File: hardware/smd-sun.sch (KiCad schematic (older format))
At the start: 18 parts, among them U1 NE555, U2 4017

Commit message: Rename all to smd-sun
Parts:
- BT1: symbol smd-star:BK-883 -> smd-sun:BK-883
- C1, C2: footprint smd-star:C_0805_2012Metric_Pad1.15x1.40mm_HandSolder -> smd-sun:C_0805_2012Metric_Pad1.15x1.40mm_HandSolder; symbol smd-star:C -> smd-sun:C
- D1, D10, D2, D3, D4, D5, D6, D7, D8, D9: footprint smd-star:LED_0805_2012Metric_Pad1.15x1.40mm_HandSolder -> smd-sun:LED_0805_2012Metric_Pad1.15x1.40mm_HandSolder; symbol smd-star:LED -> smd-sun:LED
- R1, R2, R3: footprint smd-star:R_0805_2012Metric_Pad1.15x1.40mm_HandSolder -> smd-sun:R_0805_2012Metric_Pad1.15x1.40mm_HandSolder; symbol smd-star:R -> smd-sun:R
- U1: footprint smd-star:SO-8_3.9x4.9mm_P1.27mm -> smd-sun:SO-8_3.9x4.9mm_P1.27mm; symbol smd-star:NE555 -> smd-sun:NE555
- U2: footprint smd-star:SOIC-16_3.9x9.9mm_P1.27mm -> smd-sun:SOIC-16_3.9x9.9mm_P1.27mm; symbol smd-star:4017 -> smd-sun:4017
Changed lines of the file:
@@
 $EndDescr
 $Comp
-L smd-star:NE555 U1
+L smd-sun:NE555 U1
 U 1 1 5EFD01E2
 P 3600 3350
 F 0 "U1" H 3850 3700 50  0000 C CNN
 F 1 "NE555" H 3250 3700 50  0000 C CNN
-F 2 "smd-star:SO-8_3.9x4.9mm_P1.27mm" H 3600 3350 50  0001 C CNN
+F 2 "smd-sun:SO-8_3.9x4.9mm_P1.27mm" H 3600 3350 50  0001 C CNN
 F 3 "http://www.ti.com/lit/ds/symlink/ne555.pdf" H 3600 3350 50  0001 C CNN
 	1    3600 3350
@@
 $EndComp
 $Comp
-L smd-star:4017 U2
+L smd-sun:4017 U2
 U 1 1 5EFD0D05
 P 5650 3650
 F 0 "U2" H 5900 4300 50  0000 C CNN
 F 1 "4017" H 5400 4300 50  0000 C CNN
-F 2 "smd-star:SOIC-16_3.9x9.9mm_P1.27mm" H 5650 3650 50  0001 C CNN
+F 2 "smd-sun:SOIC-16_3.9x9.9mm_P1.27mm" H 5650 3650 50  0001 C CNN
 F 3 "http://www.intersil.com/content/dam/Intersil/documents/cd40/cd4017bms-22bms.pdf" H 5650 3650 50  0001 C CNN
 	1    5650 3650
@@
 	2900 3150 3100 3150
 $Comp
-L smd-star:R R1
+L smd-sun:R R1
 U 1 1 5EFD9130
 P 4600 2900
 F 0 "R1" H 4670 2946 50  0000 L CNN
 F 1 "47k" H 4670 2855 50  0000 L CNN
-F 2 "smd-star:R_0805_2012Metric_Pad1.15x1.40mm_HandSolder" V 4530 2900 50  0001 C CNN
+F 2 "smd-sun:R_0805_2012Metric_Pad1.15x1.40mm_HandSolder" V 4530 2900 50  0001 C CNN
 F 3 "~" H 4600 2900 50  0001 C CNN
 	1    4600 2900
@@
 $EndComp
 $Comp
-L smd-star:R R2
+L smd-sun:R R2
 U 1 1 5EFDA69B
 P 4600 3650
 F 0 "R2" H 4670 3696 50  0000 L CNN
 F 1 "47k" H 4670 3605 50  0000 L CNN
-F 2 "smd-star:R_0805_2012Metric_Pad1.15x1.40mm_HandSolder" V 4530 3650 50  0001 C CNN
+F 2 "smd-sun:R_0805_2012Metric_Pad1.15x1.40mm_HandSolder" V 4530 3650 50  0001 C CNN
 F 3 "~" H 4600 3650 50  0001 C CNN
 	1    4600 3650
@@
 $EndComp
 $Comp
-L smd-star:C C1
+L smd-sun:C C1
 U 1 1 5EFDAF79
 P 2800 4050
 F 0 "C1" H 2400 4100 50  0000 L CNN
 F 1 "0.01uF" H 2400 4000 50  0000 L CNN
-F 2 "smd-star:C_0805_2012Metric_Pad1.15x1.40mm_HandSolder" H 2838 3900 50  0001 C CNN
+F 2 "smd-sun:C_0805_2012Metric_Pad1.15x1.40mm_HandSolder" H 2838 3900 50  0001 C CNN
 F 3 "~" H 2800 4050 50  0001 C CNN
 	1    2800 4050
@@
 $EndComp
 $Comp
-L smd-star:C C2
+L smd-sun:C C2
 U 1 1 5EFDE976
 P 4600 4050
 F 0 "C2" H 4715 4096 50  0000 L CNN
 F 1 "10uF" H 4715 4005 50  0000 L CNN
-F 2 "smd-star:C_0805_2012Metric_Pad1.15x1.40mm_HandSolder" H 4638 3900 50  0001 C CNN
+F 2 "smd-sun:C_0805_2012Metric_Pad1.15x1.40mm_HandSolder" H 4638 3900 50  0001 C CNN
 F 3 "~" H 4600 4050 50  0001 C CNN
 	1    4600 4050
@@
 	5650 2750 5650 2850
 $Comp
-L smd-star:LED D8
+L smd-sun:LED D8
 U 1 1 5EFF47F1
 P 7200 4200
 F 0 "D8" V 7300 4200 50  0000 R CNN
 F 1 "LED" V 7148 4083 50  0001 R CNN
-F 2 "smd-star:LED_0805_2012Metric_Pad1.15x1.40mm_HandSolder" H 7200 4200 50  0001 C CNN
+F 2 "smd-sun:LED_0805_2012Metric_Pad1.15x1.40mm_HandSolder" H 7200 4200 50  0001 C CNN
 F 3 "~" H 7200 4200 50  0001 C CNN
 	1    7200 4200
@@
 $EndComp
 $Comp
-L smd-star:LED D6
+L smd-sun:LED D6
 U 1 1 5EFF6FCA
 P 7600 4200
 F 0 "D6" V 7700 4200 50  0000 R CNN
 F 1 "LED" V 7548 4083 50  0001 R CNN
-F 2 "smd-star:LED_0805_2012Metric_Pad1.15x1.40mm_HandSolder" H 7600 4200 50  0001 C CNN
+F 2 "smd-sun:LED_0805_2012Metric_Pad1.15x1.40mm_HandSolder" H 7600 4200 50  0001 C CNN
 F 3 "~" H 7600 4200 50  0001 C CNN
 	1    7600 4200
@@
 $EndComp
 $Comp
-L smd-star:LED D5
+L smd-sun:LED D5
 U 1 1 5EFF7386
 P 7800 4200
 F 0 "D5" V 7900 4200 50  0000 R CNN
 F 1 "LED" V 7748 4083 50  0001 R CNN
-F 2 "smd-star:LED_0805_2012Metric_Pad1.15x1.40mm_HandSolder" H 7800 4200 50  0001 C CNN
+F 2 "smd-sun:LED_0805_2012Metric_Pad1.15x1.40mm_HandSolder" H 7800 4200 50  0001 C CNN
 F 3 "~" H 7800 4200 50  0001 C CNN
 	1    7800 4200
@@
 $EndComp
 $Comp
-L smd-star:LED D4
+L smd-sun:LED D4
 U 1 1 5EFF91CC
 P 8000 4200
 F 0 "D4" V 8100 4200 50  0000 R CNN
 F 1 "LED" V 7948 4083 50  0001 R CNN
-F 2 "smd-star:LED_0805_2012Metric_Pad1.15x1.40mm_HandSolder" H 8000 4200 50  0001 C CNN
+F 2 "smd-sun:LED_0805_2012Metric_Pad1.15x1.40mm_HandSolder" H 8000 4200 50  0001 C CNN
 F 3 "~" H 8000 4200 50  0001 C CNN
 	1    8000 4200
@@
 $EndComp
 $Comp
-L smd-star:LED D3
+L smd-sun:LED D3
 U 1 1 5EFF91D6
 P 8200 4200
 F 0 "D3" V 8300 4200 50  0000 R CNN
 F 1 "LED" V 8148 4083 50  0001 R CNN
-F 2 "smd-star:LED_0805_2012Metric_Pad1.15x1.40mm_HandSolder" H 8200 4200 50  0001 C CNN
+F 2 "smd-sun:LED_0805_2012Metric_Pad1.15x1.40mm_HandSolder" H 8200 4200 50  0001 C CNN
 F 3 "~" H 8200 4200 50  0001 C CNN
 	1    8200 4200
@@
 $EndComp
 $Comp
-L smd-star:LED D2
+L smd-sun:LED D2
 U 1 1 5EFF91E0
 P 8400 4200
 F 0 "D2" V 8500 4200 50  0000 R CNN
 F 1 "LED" V 8348 4083 50  0001 R CNN
-F 2 "smd-star:LED_0805_2012Metric_Pad1.15x1.40mm_HandSolder" H 8400 4200 50  0001 C CNN
+F 2 "smd-sun:LED_0805_2012Metric_Pad1.15x1.40mm_HandSolder" H 8400 4200 50  0001 C CNN
 F 3 "~" H 8400 4200 50  0001 C CNN
 	1    8400 4200
@@
 $EndComp
 $Comp
-L smd-star:LED D1
+L smd-sun:LED D1
 U 1 1 5EFF91EA
 P 8600 4200
 F 0 "D1" V 8700 4200 50  0000 R CNN
 F 1 "LED" V 8548 4083 50  0001 R CNN
-F 2 "smd-star:LED_0805_2012Metric_Pad1.15x1.40mm_HandSolder" H 8600 4200 50  0001 C CNN
+F 2 "smd-sun:LED_0805_2012Metric_Pad1.15x1.40mm_HandSolder" H 8600 4200 50  0001 C CNN
 F 3 "~" H 8600 4200 50  0001 C CNN
 	1    8600 4200
@@
 	7400 4450 7600 4450
 $Comp
-L smd-star:R R3
+L smd-sun:R R3
 U 1 1 5F0080E1
 P 6800 4600
 F 0 "R3" H 6870 4646 50  0000 L CNN
 F 1 "220R" H 6870 4555 50  0000 L CNN
-F 2 "smd-star:R_0805_2012Metric_Pad1.15x1.40mm_HandSolder" V 6730 4600 50  0001 C CNN
+F 2 "smd-sun:R_0805_2012Metric_Pad1.15x1.40mm_HandSolder" V 6730 4600 50  0001 C CNN
 F 3 "~" H 6800 4600 50  0001 C CNN
 	1    6800 4600
@@
 	7200 3850 7200 4050
 $Comp
-L smd-star:LED D9
+L smd-sun:LED D9
 U 1 1 5F0017E3
 P 7000 4200
 F 0 "D9" V 7100 4200 50  0000 R CNN
 F 1 "LED" V 6948 4083 50  0001 R CNN
-F 2 "smd-star:LED_0805_2012Metric_Pad1.15x1.40mm_HandSolder" H 7000 4200 50  0001 C CNN
+F 2 "smd-sun:LED_0805_2012Metric_Pad1.15x1.40mm_HandSolder" H 7000 4200 50  0001 C CNN
 F 3 "~" H 7000 4200 50  0001 C CNN
 	1    7000 4200
@@
 $EndComp
 $Comp
-L smd-star:LED D10
+L smd-sun:LED D10
 U 1 1 5F001F99
 P 6800 4200
 F 0 "D10" V 6900 4200 50  0000 R CNN
 F 1 "LED" V 6748 4083 50  0001 R CNN
-F 2 "smd-star:LED_0805_2012Metric_Pad1.15x1.40mm_HandSolder" H 6800 4200 50  0001 C CNN
+F 2 "smd-sun:LED_0805_2012Metric_Pad1.15x1.40mm_HandSolder" H 6800 4200 50  0001 C CNN
 F 3 "~" H 6800 4200 50  0001 C CNN
 	1    6800 4200
@@
 LED9
 $Comp
-L smd-star:LED D7
+L smd-sun:LED D7
 U 1 1 5EFF6B7E
 P 7400 4200
 F 0 "D7" V 7500 4200 50  0000 R CNN
 F 1 "LED" V 7348 4083 50  0001 R CNN
-F 2 "smd-star:LED_0805_2012Metric_Pad1.15x1.40mm_HandSolder" H 7400 4200 50  0001 C CNN
+F 2 "smd-sun:LED_0805_2012Metric_Pad1.15x1.40mm_HandSolder" H 7400 4200 50  0001 C CNN
 F 3 "~" H 7400 4200 50  0001 C CNN
 	1    7400 4200
@@
 LED10
 $Comp
-L smd-star:BK-883 BT1
+L smd-sun:BK-883 BT1
 U 1 1 5EFF5419
 P 1500 3650

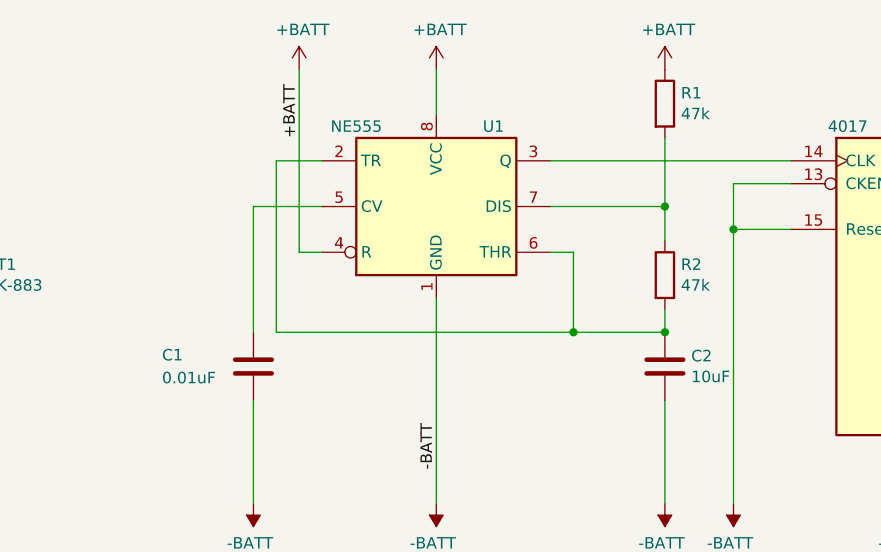
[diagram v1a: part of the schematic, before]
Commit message: Fix resistor values Enlarge SOIC pads to make soldering easier
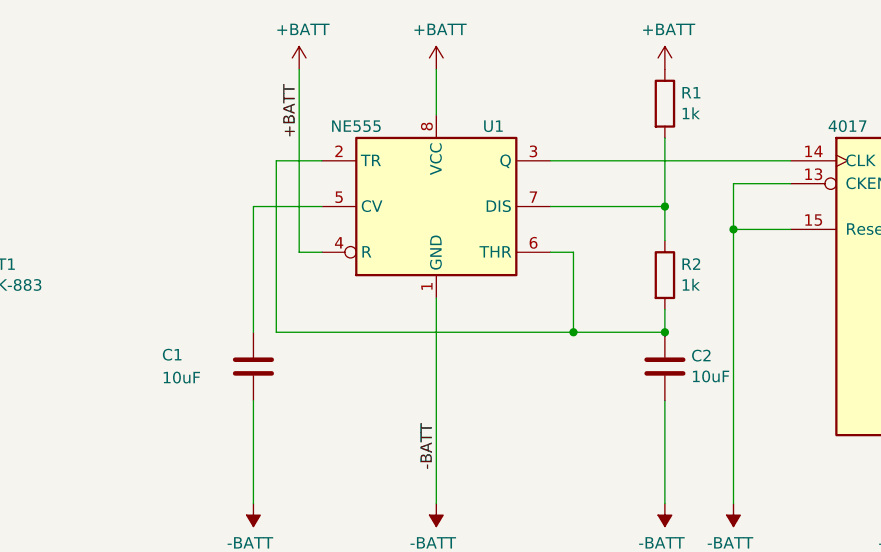
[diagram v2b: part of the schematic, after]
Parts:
- C1: value 0.01uF -> 10uF
- R1, R2: value 47k -> 1k
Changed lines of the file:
@@
 P 4600 2900
 F 0 "R1" H 4670 2946 50  0000 L CNN
-F 1 "47k" H 4670 2855 50  0000 L CNN
+F 1 "1k" H 4670 2855 50  0000 L CNN
 F 2 "smd-sun:R_0805_2012Metric_Pad1.15x1.40mm_HandSolder" V 4530 2900 50  0001 C CNN
 F 3 "~" H 4600 2900 50  0001 C CNN
@@
 P 4600 3650
 F 0 "R2" H 4670 3696 50  0000 L CNN
-F 1 "47k" H 4670 3605 50  0000 L CNN
+F 1 "1k" H 4670 3605 50  0000 L CNN
 F 2 "smd-sun:R_0805_2012Metric_Pad1.15x1.40mm_HandSolder" V 4530 3650 50  0001 C CNN
 F 3 "~" H 4600 3650 50  0001 C CNN
@@
 P 2800 4050
 F 0 "C1" H 2400 4100 50  0000 L CNN
-F 1 "0.01uF" H 2400 4000 50  0000 L CNN
+F 1 "10uF" H 2400 4000 50  0000 L CNN
 F 2 "smd-sun:C_0805_2012Metric_Pad1.15x1.40mm_HandSolder" H 2838 3900 50  0001 C CNN
 F 3 "~" H 2800 4050 50  0001 C CNN

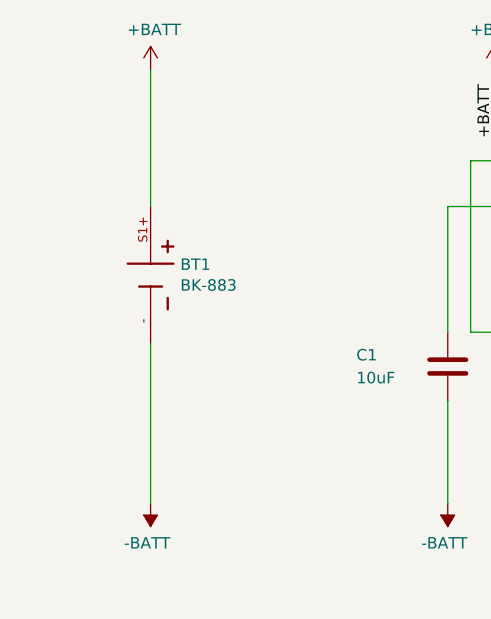
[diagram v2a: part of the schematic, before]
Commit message: Add test points
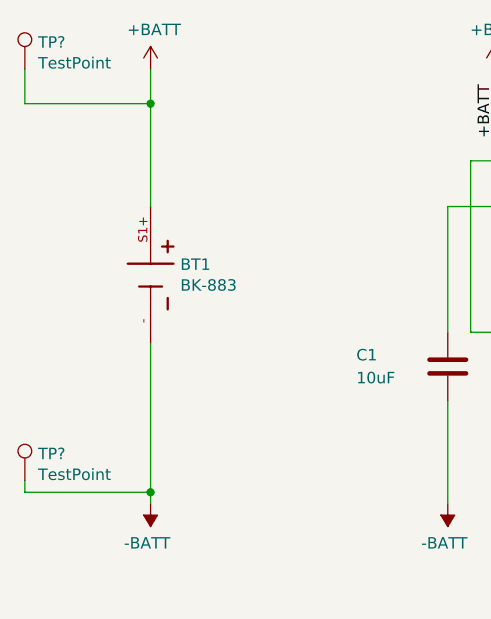
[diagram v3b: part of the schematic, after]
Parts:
- added TP? (x2): TestPoint, symbol smd-sun:TestPoint
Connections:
- net +BATT: now also TP?.1
- net -BATT: now also TP?.1
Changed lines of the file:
@@
 $EndComp
 $Comp
-L power:+BATT #PWR?
+L power:+BATT #PWR0101
 U 1 1 5EFF6E79
 P 1500 2750
-F 0 "#PWR?" H 1500 2600 50  0001 C CNN
+F 0 "#PWR0101" H 1500 2600 50  0001 C CNN
 F 1 "+BATT" H 1515 2923 50  0000 C CNN
 F 2 "" H 1500 2750 50  0001 C CNN
@@
 $EndComp
 $Comp
-L power:-BATT #PWR?
+L power:-BATT #PWR0102
 U 1 1 5EFF8919
 P 1500 4650
-F 0 "#PWR?" H 1500 4500 50  0001 C CNN
+F 0 "#PWR0102" H 1500 4500 50  0001 C CNN
 F 1 "-BATT" H 1515 4823 50  0000 C CNN
 F 2 "" H 1500 4650 50  0001 C CNN
@@
 $EndComp
 Wire Wire Line
-	1500 3950 1500 4650
+	1500 3950 1500 4600
 Wire Wire Line
-	1500 2750 1500 3350
+	1500 2750 1500 2900
+$Comp
+L smd-sun:TestPoint TP?
+U 1 1 5FD86380
+P 950 2750
+F 0 "TP?" H 1008 2868 50  0000 L CNN
+F 1 "TestPoint" H 1008 2777 50  0000 L CNN
+F 2 "" H 1150 2750 50  0001 C CNN
+F 3 "~" H 1150 2750 50  0001 C CNN
+	1    950  2750
+	1    0    0    -1
+$EndComp
+$Comp
+L smd-sun:TestPoint TP?
+U 1 1 5FD86899
+P 950 4550
+F 0 "TP?" H 1008 4668 50  0000 L CNN
+F 1 "TestPoint" H 1008 4577 50  0000 L CNN
+F 2 "" H 1150 4550 50  0001 C CNN
+F 3 "~" H 1150 4550 50  0001 C CNN
+	1    950  4550
+	1    0    0    -1
+$EndComp
+Wire Wire Line
+	950  2750 950  2900
+Wire Wire Line
+	950  2900 1500 2900
+Connection ~ 1500 2900
+Wire Wire Line
+	1500 2900 1500 3350
+Wire Wire Line
+	1500 4600 950  4600
+Wire Wire Line
+	950  4600 950  4550
+Connection ~ 1500 4600
+Wire Wire Line
+	1500 4600 1500 4650
 $EndSCHEMATC

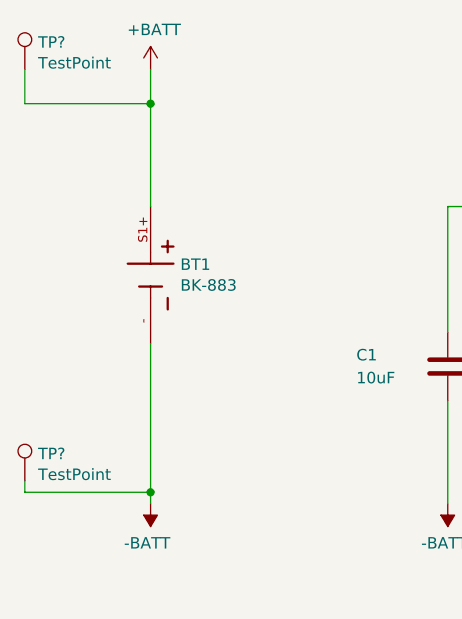
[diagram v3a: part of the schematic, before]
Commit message: Add two test point for bringup, fix errata from Jun2020
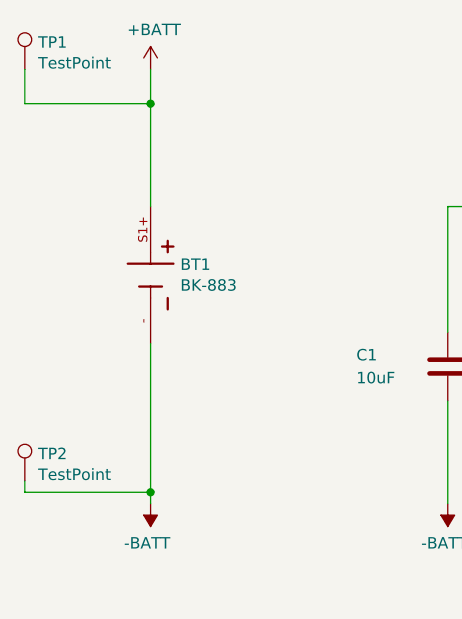
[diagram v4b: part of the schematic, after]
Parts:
- BT1: footprint BAT_BK-883 -> smd-sun:BAT_BK-883
- TP1, TP2: renamed from TP?; footprint (none) -> smd-sun:TestPoint_Pad_D3.0mm
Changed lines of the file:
@@
 F 0 "BT1" V 1454 3780 50  0000 L CNN
 F 1 "BK-883" V 1545 3780 50  0000 L CNN
-F 2 "BAT_BK-883" H 1500 3650 50  0001 L BNN
+F 2 "smd-sun:BAT_BK-883" H 1500 3650 50  0001 L BNN
 F 3 "L" H 1500 3650 50  0001 L BNN
 F 4 "MPD" H 1500 3650 50  0001 L BNN "Field4"
@@
 	1500 2750 1500 2900
 $Comp
-L smd-sun:TestPoint TP?
+L smd-sun:TestPoint TP1
 U 1 1 5FD86380
 P 950 2750
-F 0 "TP?" H 1008 2868 50  0000 L CNN
+F 0 "TP1" H 1008 2868 50  0000 L CNN
 F 1 "TestPoint" H 1008 2777 50  0000 L CNN
-F 2 "" H 1150 2750 50  0001 C CNN
+F 2 "smd-sun:TestPoint_Pad_D3.0mm" H 1150 2750 50  0001 C CNN
 F 3 "~" H 1150 2750 50  0001 C CNN
 	1    950  2750
@@
 $EndComp
 $Comp
-L smd-sun:TestPoint TP?
+L smd-sun:TestPoint TP2
 U 1 1 5FD86899
 P 950 4550
-F 0 "TP?" H 1008 4668 50  0000 L CNN
+F 0 "TP2" H 1008 4668 50  0000 L CNN
 F 1 "TestPoint" H 1008 4577 50  0000 L CNN
-F 2 "" H 1150 4550 50  0001 C CNN
+F 2 "smd-sun:TestPoint_Pad_D3.0mm" H 1150 4550 50  0001 C CNN
 F 3 "~" H 1150 4550 50  0001 C CNN
 	1    950  4550
